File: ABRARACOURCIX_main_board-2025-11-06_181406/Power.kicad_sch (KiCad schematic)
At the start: 32 parts, among them J2 XT60PW-M, J3 XT60PW-M, K1 Relai_T9GV1L14-5, Q2 NTR4101PT1G, Q3 MMBT3904, U2 Current_sens_ACS712ELCTR-20A-T, U3 AZ1117CH-3.3TRG1, U4 Xl4015, U6 LMC6482, U7 LMC6482

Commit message: Modifs au circuit d'alim
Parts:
- removed BUZ_D2: BAT54T1G, Diode_SMD:D_SOD-123, symbol Diode:1N6858UR
- removed BUZ_R3: 1k5, Resistor_SMD:R_1206_3216Metric_Pad1.30x1.75mm_HandSolder, symbol Device:R
- removed K1: Relai_T9GV1L14-5, Librairie_footprint:Relai_30A_T9GV1L14-5_TEC, symbol GAUL_ABRARACOURCIX:Relai_T9GV1L14-5
- removed Q3: MMBT3904, Package_TO_SOT_SMD:SOT-23-3, symbol Simulation_SPICE:NPN
- removed U4: Xl4015, Librairie_footprint:Buck_breakout_Xl4015, symbol GAUL_ABRARACOURCIX:Buck_Xl4015_breakout
- added J1, J12: Conn_01x02_Pin, Librairie_footprint:MTA_100_2pos, symbol Connector:Conn_01x02_Pin
- added Q4: IKD15N60R, Package_TO_SOT_SMD:TO-252-2, symbol Device:Q_NIGBT_CEG
- added Q6: NTR4101PT1G, Package_TO_SOT_SMD:SOT-23-3, symbol Simulation_SPICE:PMOS
- added R18: 1k5, symbol Device:R
- added R2: 10k, symbol Device:R
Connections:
- net +5V: now also J12.1 (Pin_1), Q6.1 (D)
- net GND: now also J1.2 (Pin_2), J12.2 (Pin_2), R2.2
- net Motor_switch: now also R18.2
- net VBAT: now also Q4.2 (E)
- net VBAT_sense: now also J1.1 (Pin_1)
- net at Q2.1 (D), U2.3 (IP-__1), U2.4 (IP-): now also Q4.1 (C)
- new net: Q6.2 (G), R18.1
- new net: Q4.3 (G), Q6.3 (S), R2.1
- no-connect marks 5 -> 4
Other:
- note added: "20 AMP trace"
- note added: "IGBT used as high current switch Off by default with p-channel mosfet (if Motor_switch signal is low or 5V goes down, no current goes through IGBT)"
- note added: "IKD15N60R"
- note added: "To buck converter"
- note removed: "Max 30A DC"
- note removed: "Volume fixe (maximal) à cause de la résistance fixe de 50 Ohm"

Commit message: Modif circuit d'arrêt
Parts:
- removed Q4: IKD15N60R, Package_TO_SOT_SMD:TO-252-2, symbol Device:Q_NIGBT_CEG
- removed Q6: NTR4101PT1G, Package_TO_SOT_SMD:SOT-23-3, symbol Simulation_SPICE:PMOS
- added J7: XT60PW-F, Librairie_footprint:AMASS_XT60PW-F, symbol GAUL_ABRARACOURCIX:XT60PW-F
- added Q3: NPN, symbol Simulation_SPICE:NPN
- added Q5: PNP, symbol Simulation_SPICE:PNP
- added Q6: IKD15N60R, Package_TO_SOT_SMD:TO-252-2, symbol Device:Q_NIGBT_CEG
- added R19: 10k, symbol Device:R
- added R20: 1k5, symbol Device:R
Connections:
- net GND: now also J7.S1 (SHIELD), J7.S2 (SHIELD), Q3.3 (E), Q6.2 (E)
- net at R18.1: now also Q3.2 (B)
- net at R2.1: now also Q5.1 (C), Q6.3 (G)
- net at Q2.1 (D), U2.3 (IP-__1), U2.4 (IP-): now also J7.2
- new net: J7.1, Q5.3 (E), Q6.1 (C), R19.1
- new net: Q3.1 (C), R19.2, R20.2
- new net: Q5.2 (B), R20.1
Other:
- note added: "Output to ESC Max 30 A 15 V XT60 Female"
- moved on the sheet: C1, C2, C3, D1, J1, J12, R1, R18, R2, U3

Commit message: Placement des composantes 95%
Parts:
- Q3: value NPN -> NPN-DSS20201L-7; footprint (none) -> Package_TO_SOT_SMD:SOT-23; Digikey (none) -> https://www.digikey.ca/en/products/detail/diodes-incorporat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
- Q5: value PNP -> DSS20200L-7-PNP; footprint (none) -> Package_TO_SOT_SMD:SOT-23-3; Digikey (none) -> https://www.digikey.ca/en/products/detail/diodes-incorporat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
- R18, R19, R2, R20: footprint (none) -> Resistor_SMD:R_1206_3216Metric_Pad1.30x1.75mm_HandSolder
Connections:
- net GND: now also Q3.E, Q6.E; no longer Q3.3 (E), Q6.2 (E)
- net VBAT_sense: now also Q2.S; no longer Q2.3 (S)
- net at J7.1, R19.1: now also Q5.E, Q6.C; no longer Q5.3 (E), Q6.1 (C)
- net at R18.1: now also Q3.B; no longer Q3.2 (B)
- net at DZ1.2 (A), PWR_R5.1: now also Q2.G; no longer Q2.2 (G)
- net at J7.2, U2.3 (IP-__1), U2.4 (IP-): now also Q2.D; no longer Q2.1 (D)
- net at R19.2, R20.2: now also Q3.C; no longer Q3.1 (C)
- net at R20.1: now also Q5.B; no longer Q5.2 (B)
- new net: Q5.C, Q6.G, R2.1
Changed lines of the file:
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@@
 	(text "IGBT used as high current switch\nOff by default with p-channel mosfet\n(if Motor_switch signal is low or \n5V goes down, no current goes through IGBT)"
 		(exclude_from_sim no)
-		(at 185.928 90.932 0)
+		(at 207.772 71.882 0)
 		(effects
 			(font
@@
 	)
 	(image
-		(at 397.51 123.19)
+		(at 386.08 107.95)
 		(data "iVBORw0KGgoAAAANSUhEUgAACAAAAAKuCAIAAAC6o2u3AAAAA3NCSVQICAjb4U/gAAAgAElEQVR4"
 			"nOzdd5BlV3Uv/u9OJ9zUt3NO05Nz1sxImpFQTkggiWTsH8akBwbbQGE/v4eNqefAM8Y2trExGDBY"
@@
 		)
 		(property "Footprint" "Package_TO_SOT_SMD:TO-252-2"
-			(at 204.47 43.18 0)
+			(at 206.502 33.274 0)
 			(effects
 				(font
@@
 		)
 		(property "Datasheet" "https://www.infineon.com/assets/row/public/documents/60/49/infineon-ikd15n60r-ds-en.pdf?fileId=db3a30433c5c92fb013c5e03026003b2"
-			(at 209.55 45.72 0)
+			(at 210.058 33.274 0)
 			(effects
 				(font
@@
 		)
 		(property "Description" "N-IGBT transistor, collector/emitter/gate"
-			(at 209.55 45.72 0)
+			(at 209.55 33.02 0)
 			(effects
 				(font
@@
 		)
 		(property "Digikey" "https://www.digikey.ca/en/products/detail/infineon-technologies/IKD15N60RATMA1/6131387"
-			(at 209.55 45.72 0)
+			(at 209.042 33.782 0)
 			(effects
 				(font
@@
 			)
 		)
-		(pin "3"
+		(pin "C"
 		)
-		(pin "2"
+		(pin "G"
 		)
-		(pin "1"
+		(pin "E"
 		)
 		(instances
@@
 			)
 		)
-		(property "Footprint" ""
+		(property "Footprint" "Resistor_SMD:R_1206_3216Metric_Pad1.30x1.75mm_HandSolder"
 			(at 262.89 52.578 90)
 			(effects
@@
 			)
 		)
-		(property "Footprint" ""
+		(property "Footprint" "Resistor_SMD:R_1206_3216Metric_Pad1.30x1.75mm_HandSolder"
 			(at 226.822 52.07 90)
 			(effects
@@
 		)
 		(property "Footprint" "Package_TO_SOT_SMD:SOT-23-3"
-			(at 139.7 55.88 0)
+			(at 127.762 51.562 0)
 			(effects
 				(font
@@
 		)
 		(property "Description" "P-MOSFET transistor, drain/source/gate"
-			(at 142.24 60.96 0)
+			(at 129.54 56.388 0)
 			(effects
 				(font
@@
 		)
 		(property "Digikey" "NTR4101PT1GOSCT-ND"
-			(at 142.24 60.96 0)
+			(at 128.27 54.864 0)
 			(effects
 				(font
@@
 			)
 		)
-		(pin "1"
+		(pin "D"
 		)
-		(pin "3"
+		(pin "G"
 		)
-		(pin "2"
+		(pin "S"
 		)
 		(instances
@@
 			)
 		)
-		(property "Footprint" ""
+		(property "Footprint" "Resistor_SMD:R_1206_3216Metric_Pad1.30x1.75mm_HandSolder"
 			(at 247.142 36.83 90)
 			(effects
@@
 			)
 		)
-		(property "Value" "NPN"
-			(at 246.38 52.0699 0)
+		(property "Value" "NPN-DSS20201L-7"
+			(at 268.732 55.88 0)
 			(effects
 				(font
@@
 			)
 		)
-		(property "Footprint" ""
+		(property "Footprint" "Package_TO_SOT_SMD:SOT-23"
 			(at 187.96 50.8 0)
 			(effects
@@
 			)
 		)
-		(property "Datasheet" "https://ngspice.sourceforge.io/docs/ngspice-html-manual/manual.xhtml#cha_BJTs"
+		(property "Datasheet" "https://www.diodes.com/assets/Datasheets/ds31605.pdf"
 			(at 187.96 50.8 0)
 			(effects
@@
 			)
 		)
-		(pin "2"
+		(property "Digikey" "https://www.digikey.ca/en/products/detail/diodes-incorporated/DSS20201L-7/2044515"
+			(at 251.46 50.8 0)
+			(effects
+				(font
+					(size 1.27 1.27)
+				)
+				(hide yes)
+			)
 		)
-		(pin "1"
+		(pin "C"
 		)
-		(pin "3"
+		(pin "E"
+		)
+		(pin "B"
 		)
 		(instances
@@
 			)
 		)
-		(property "Footprint" ""
+		(property "Footprint" "Resistor_SMD:R_1206_3216Metric_Pad1.30x1.75mm_HandSolder"
 			(at 242.57 42.418 90)
 			(effects
@@
 			)
 		)
-		(property "Value" "PNP"
+		(property "Value" "DSS20200L-7-PNP"
 			(at 226.06 39.3701 0)
 			(effects
@@
 			)
 		)
-		(property "Footprint" ""
+		(property "Footprint" "Package_TO_SOT_SMD:SOT-23-3"
 			(at 195.58 40.64 0)
 			(effects
@@
 			)
 		)
-		(property "Datasheet" "https://ngspice.sourceforge.io/docs/ngspice-html-manual/manual.xhtml#cha_BJTs"
+		(property "Datasheet" "https://www.diodes.com/assets/Datasheets/ds31604.pdf"
 			(at 195.58 40.64 0)
 			(effects
@@
 			)
 		)
-		(pin "2"
+		(property "Digikey" "https://www.digikey.ca/en/products/detail/diodes-incorporated/DSS20200L-7/2044514"
+			(at 231.14 40.64 0)
+			(effects
+				(font
+					(size 1.27 1.27)
+				)
+				(hide yes)
+			)
 		)
-		(pin "1"
+		(pin "C"
 		)
-		(pin "3"
+		(pin "E"
+		)
+		(pin "B"
 		)
 		(instances

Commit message: Documentation de composantes
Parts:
- removed U6: LMC6482, Librairie_footprint:SOIC127P599X175-8N, symbol Amplifier_Operational:LMC6482
- added U4: LMC6482AIMX/NOPB, Librairie_footprint:SOIC127P599X175-8N, symbol Amplifier_Operational:LMC6482
- U7: value LMC6482 -> LMC6482AIMX/NOPB; Digikey (none) -> https://www.digikey.ca/en/products/detail/texas-instruments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; Part number (none) -> LMC6482AIMX/NOPBCT-ND
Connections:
- net +3.3V: now also U4.8 (V+)
- net GND: now also U4.4 (V-)
- net 20A_pre_switch: now reaches J2.2 (-), J3.1 (+)
- net at R15.2, R16.1: now also U4.5 (+)
- net at R12.1: now also U4.6 (-), U4.7

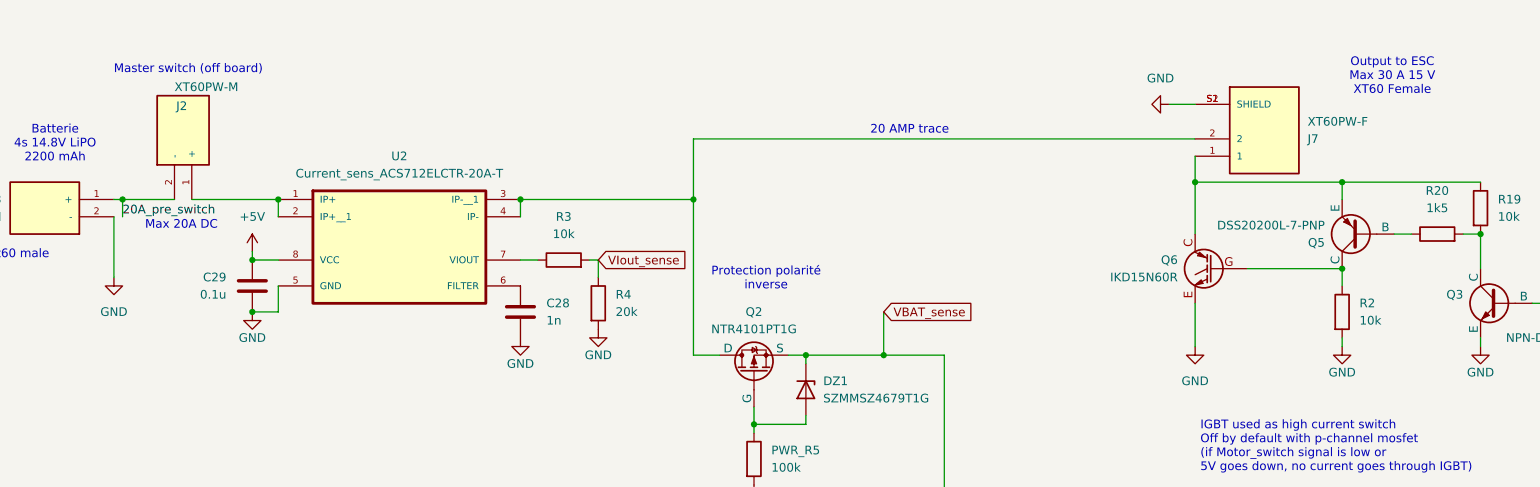
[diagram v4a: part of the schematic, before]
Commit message: Déplacement des mounting holes et début du routing
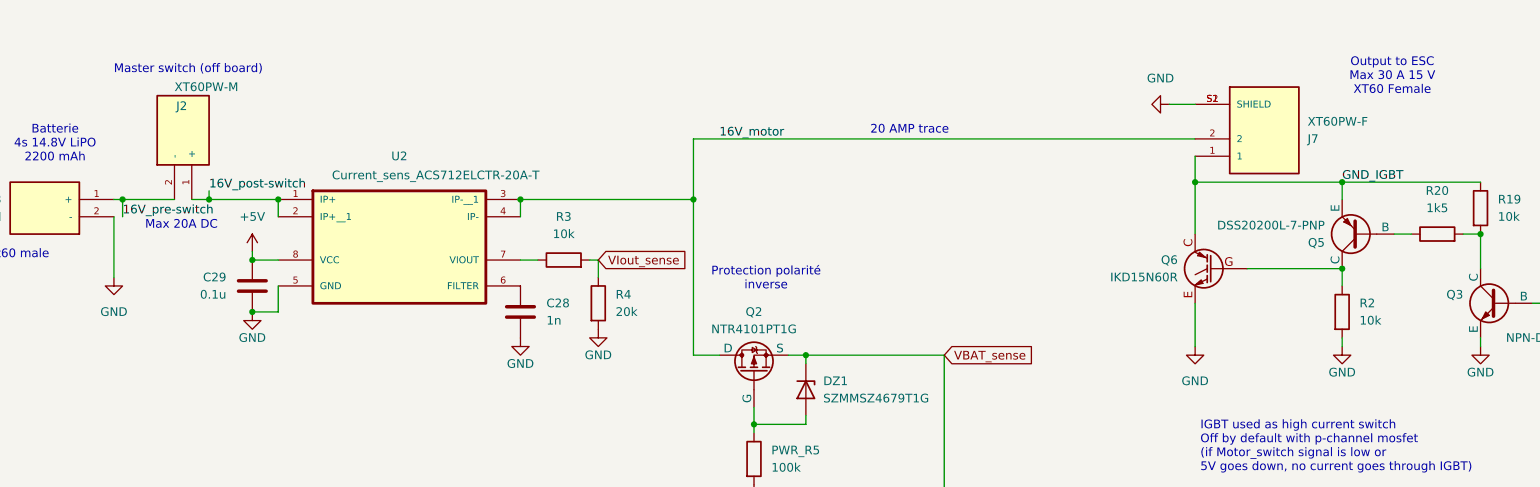
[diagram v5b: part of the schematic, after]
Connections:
- net GND_IGBT: now reaches J7.1, Q5.E, Q6.C, R19.1
- net 16V_motor: now reaches J7.2, Q2.D, U2.3 (IP-__1), U2.4 (IP-)
- net 16V_post-switch: now reaches J2.1 (+), U2.1 (IP+), U2.2 (IP+__1)
- net 20A_pre_switch renamed 16V_pre-switch
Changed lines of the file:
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@@
 	)
 	(junction
-		(at 161.29 58.42)
-		(diameter 0)
-		(color 0 0 0 0)
-	)
-	(junction
 		(at 133.35 35.56)
 		(diameter 0)
@@
 	)
 	(junction
+		(at 62.23 35.56)
+		(diameter 0)
+		(color 0 0 0 0)
+	)
+	(junction
 		(at 259.08 109.22)
 		(diameter 0)
@@
 	(wire
 		(pts
-			(xy 59.69 35.56) (xy 72.39 35.56)
+			(xy 59.69 35.56) (xy 62.23 35.56)
 		)
 		(stroke
@@
 	(wire
 		(pts
+			(xy 62.23 34.29) (xy 62.23 35.56)
+		)
+		(stroke
+			(width 0)
+			(type default)
+		)
+	)
+	(wire
+		(pts
 			(xy 228.6 48.26) (xy 228.6 45.72)
 		)
@@
 	(wire
 		(pts
-			(xy 161.29 58.42) (xy 170.18 58.42)
+			(xy 207.01 33.02) (xy 207.01 40.64)
 		)
 		(stroke
@@
 	(wire
 		(pts
-			(xy 207.01 33.02) (xy 207.01 40.64)
+			(xy 236.22 40.64) (xy 238.76 40.64)
 		)
 		(stroke
@@
 	(wire
 		(pts
-			(xy 236.22 40.64) (xy 238.76 40.64)
+			(xy 195.58 143.51) (xy 196.85 143.51)
 		)
 		(stroke
@@
 	(wire
 		(pts
-			(xy 195.58 143.51) (xy 196.85 143.51)
+			(xy 170.18 109.22) (xy 170.18 58.42)
 		)
 		(stroke
@@
 	(wire
 		(pts
-			(xy 170.18 109.22) (xy 170.18 58.42)
+			(xy 237.49 140.97) (xy 232.41 140.97)
 		)
 		(stroke
@@
 	(wire
 		(pts
-			(xy 237.49 140.97) (xy 232.41 140.97)
+			(xy 66.04 127) (xy 82.55 127)
 		)
 		(stroke
@@
 	(wire
 		(pts
-			(xy 66.04 127) (xy 82.55 127)
+			(xy 62.23 35.56) (xy 72.39 35.56)
 		)
 		(stroke
@@
 	(wire
 		(pts
-			(xy 149.86 58.42) (xy 161.29 58.42)
+			(xy 149.86 58.42) (xy 170.18 58.42)
 		)
 		(stroke
@@
 	(wire
 		(pts
-			(xy 161.29 52.07) (xy 161.29 58.42)
-		)
-		(stroke
-			(width 0)
-			(type default)
-		)
-	)
-	(wire
-		(pts
 			(xy 81.28 157.48) (xy 101.6 157.48)
 		)
@@
 		)
 	)
-	(label "20A_pre_switch"
+	(label "16V_motor"
+		(at 137.16 26.67 0)
+		(effects
+			(font
+				(size 1.27 1.27)
+			)
+			(justify left bottom)
+		)
+	)
+	(label "16V_pre-switch"
 		(at 49.53 38.1 0)
 		(effects
@@
 		)
 	)
+	(label "GND_IGBT"
+		(at 228.6 33.02 0)
+		(effects
+			(font
+				(size 1.27 1.27)
+			)
+			(justify left bottom)
+		)
+	)
+	(label "16V_post-switch"
+		(at 62.23 34.29 0)
+		(effects
+			(font
+				(size 1.27 1.27)
+			)
+			(justify left bottom)
+		)
+	)
 	(global_label "VBAT_sense"
 		(shape input)
@@
 	(global_label "VBAT_sense"
 		(shape input)
-		(at 161.29 52.07 0)
+		(at 170.18 58.42 0)
 		(fields_autoplaced yes)
 		(effects
@@
 		)
 		(property "Intersheetrefs" "${INTERSHEET_REFS}"
-			(at 175.04 52.07 0)
+			(at 183.93 58.42 0)
 			(effects
 				(font
@@
 		(on_board yes)
 		(dnp no)
-		(fields_autoplaced yes)
 		(property "Reference" "U2"
 			(at 90.17 29.21 0)
@@
 		)
 		(property "Value" "Current_sens_ACS712ELCTR-20A-T"
-			(at 90.17 31.75 0)
+			(at 95.504 32.004 0)
 			(effects
 				(font

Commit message: Routing terminé (v1)
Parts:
- renumbered C29 to C16, C28 to C17, C3 to C18, C2 to C19, C30 to C20, C1 to C21, D1 to D2, J3 to J10, J1 to J11, J2 to J8, J7 to J9, PWR_R5 to PWR_R1, Q5 to Q2, Q6 to Q3, Q3 to Q4, Q2 to Q5, R18 to R10, R2 to R11, R11 to R12, R15 to R13, R12 to R14, R1 to R15, R13 to R17, R14 to R18, R8 to R19, R9 to R20, R19 to R6, R20 to R7, R3 to R8, R4 to R9, U2 to U3, U3 to U4, U4 to U5, U7 to U6
